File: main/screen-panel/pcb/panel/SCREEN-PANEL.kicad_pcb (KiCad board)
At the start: 2 copper layers, 170 x 100 mm, 48 parts, among them CN1 SM02B-SRSS-TB, CN2 SM04B-SRSS-TB, CN3 SM04B-SRSS-TB, U1 USB2422/MJ, X1 24Mhz

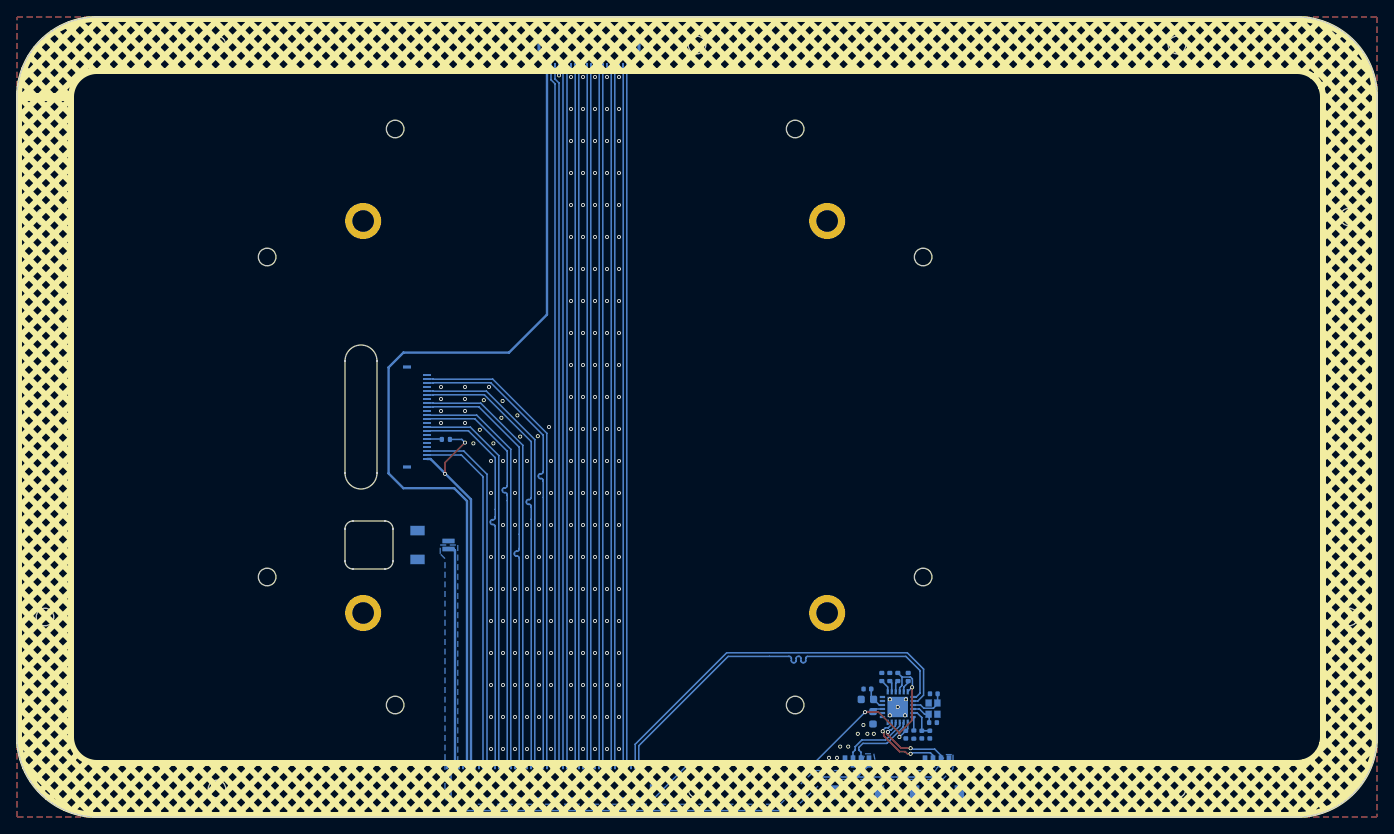
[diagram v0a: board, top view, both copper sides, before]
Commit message: rerouted the screen panel pairs
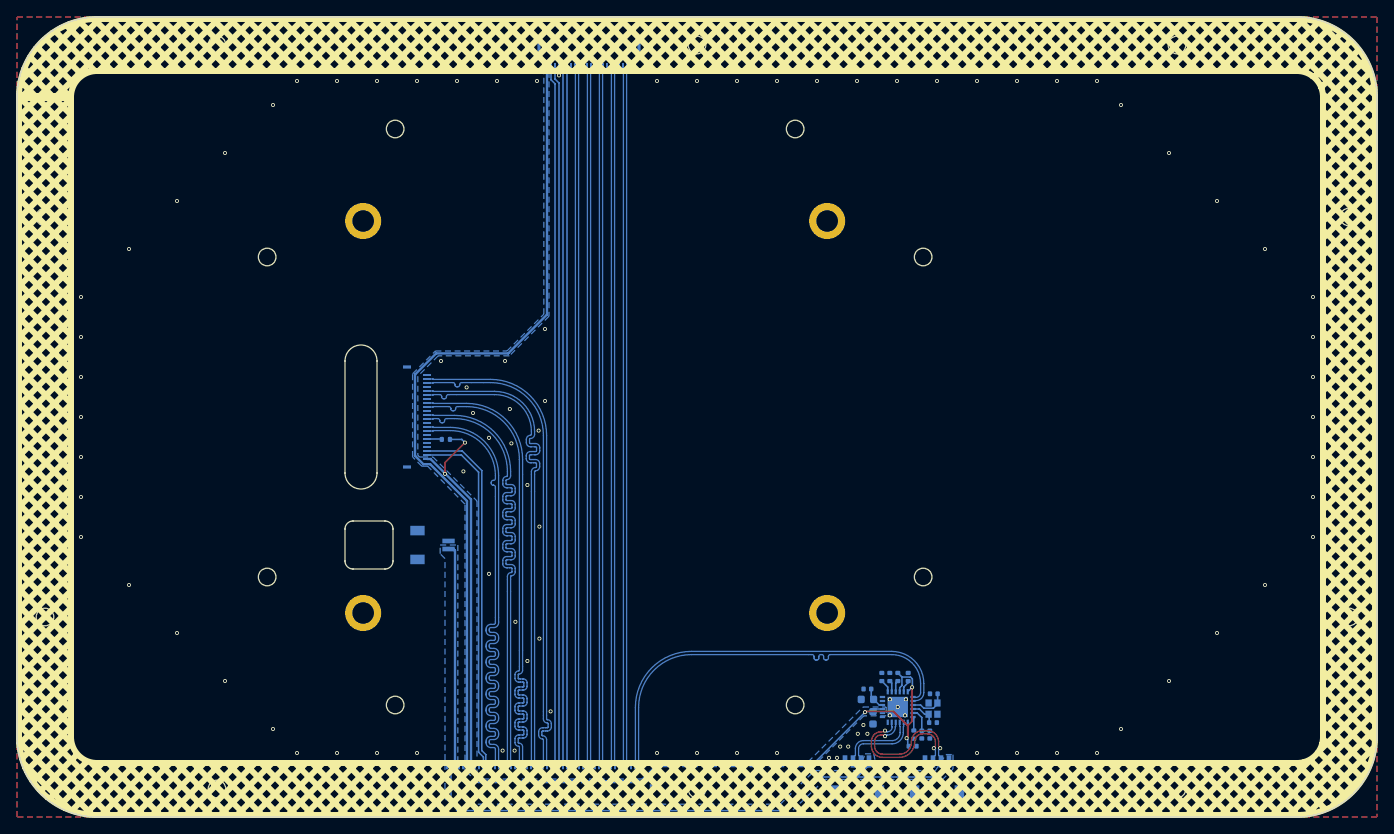
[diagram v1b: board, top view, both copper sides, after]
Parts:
- G***: footprint UUID:17fc90c1-7042-45bd-8d3c-3143bec1a9da -> UUID:785913dc-9be3-4e90-8ce0-edc40dcda3d7
- moved C1 1.68 mm to (226.9, 171.2), turned to 180 degrees
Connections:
- FPC2 pad 4: unconnected-(FPC2-Pad4) -> GND
- FPC2 pad 5: unconnected-(FPC2-Pad5) -> GND
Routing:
- net /display-sw/MPI1_D3_P: track 49.3 -> 61.2 mm
- net /display-sw/MPI1_D3_N: track 49.4 -> 61.2 mm
- net +3V3: track 239.3 -> 229.5 mm
- net /display-sw/MPI1_D2_P: track 51.9 -> 61.4 mm
- net /display-sw/MPI1_D2_N: track 51.9 -> 61.4 mm
- net /USB2.0HUB/M1_USB_DP: track 10.5 -> 18.5 mm
- net /USB2.0HUB/M1_USB_DN: track 10.6 -> 18.5 mm
- net /display-sw/MPI1_C_P: track 54.3 -> 61.5 mm
- net /display-sw/MPI1_C_N: track 54.4 -> 61.5 mm
- net /display-sw/MPI1_D1_P: track 56.8 -> 61.6 mm
- net /display-sw/MPI1_D1_N: track 56.9 -> 61.7 mm
- net /USB2.0HUB/USBHUB_DN: track 49.3 -> 52.3 mm
- net /USB2.0HUB/USBHUB_DP: track 49.3 -> 52.4 mm
- net /display-sw/MPI1_D0_P: track 59.4 -> 61.6 mm
- net /display-sw/MPI1_D0_N: track 59.5 -> 61.6 mm
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- added copper zone on B.Cu, net +3V3
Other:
- board text added: "0.2PT"
- board text added: "2026-0504-2006"
- board text added: "785..a3d7"
- board text removed: "0.1PT"
- board text removed: "17f..c1a9"
- board text removed: "2026-0429-1006"
